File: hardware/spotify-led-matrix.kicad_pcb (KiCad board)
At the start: 2 copper layers, 192.1 x 264.1 mm, 78 parts, among them J1 +5V, J2 DISPLAY_IN, J4 DISPLAY_OUT, J5 USB_C_Receptacle_USB2.0, Q1 IRLML6244TRPBF, Q2 SS8050-G, Q3 SS8050-G, Q4 IRLML6244TRPBF, Q5 IRLML6244TRPBF, Q6 IRLML6244TRPBF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

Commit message: Reorganized files again: Wanted to push to backup everything.
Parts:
- moved Q2 17.8 mm to (85.5, 332.4)
- moved Q3 17.4 mm to (90.5, 332.4)
- moved R20 12.8 mm to (88.0, 336.3), turned to 0 degrees
- moved R19 12.5 mm to (82.0, 333.8), turned to -90 degrees

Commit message: update
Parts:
- moved D2 128.5 mm to (90.5, 390.2)
- moved D4 128.5 mm to (113.1, 390.2)
- moved D8 128.5 mm to (124.5, 390.2)
- moved D3 128.5 mm to (101.8, 390.2)
- moved Q1 128.5 mm to (89.1, 386.7)
- moved Q7 128.5 mm to (123.1, 386.7)
- moved Q8 128.5 mm to (112.1, 386.7)
- moved Q9 128.5 mm to (100.6, 386.7)
- moved R13 128.5 mm to (108.6, 384.2)
- moved R15 128.5 mm to (119.6, 384.1)
- moved R17 128.5 mm to (85.6, 384.2)
- moved R2 128.5 mm to (97.1, 384.1)
- moved R3 128.5 mm to (104.6, 386.2)
- moved R6 128.5 mm to (116.1, 386.1)
- moved R7 128.5 mm to (127.1, 386.2)
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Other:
- board size 192.1 x 264.1 mm -> 192 x 264 mm

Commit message: worked on the layout
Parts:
- moved C10 174.4 mm to (230.3, 251.2), turned to 0 degrees
- moved C6 172.3 mm to (230.3, 267.8), turned to 0 degrees
- moved R12 167.3 mm to (224.1, 280.8), turned to 0 degrees
- moved SW2 167.1 mm to (231.1, 276.1), turned to 90 degrees
- moved SW3 166.9 mm to (231.1, 259.4), turned to 90 degrees
- moved R8 164.9 mm to (224.1, 264.1), turned to 0 degrees
- moved R19 163.8 mm to (181.6, 293.1)
- moved Q2 162.5 mm to (184.0, 292.0)
- moved R20 162.0 mm to (185.4, 295.0)
- moved Q3 160.6 mm to (186.8, 292.1)
- moved C8 154.8 mm to (164.8, 290.5), turned to 90 degrees
- moved C9 150.6 mm to (161.8, 290.5), turned to 90 degrees
- moved J5 150.6 mm to (153.0, 317.0)
- moved C17 147.7 mm to (156.8, 305.0), turned to 0 degrees
- moved C21 147.6 mm to (158.8, 295.9), turned to -90 degrees
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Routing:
- net +3V3: track 0.25 -> 19.4 mm
- net /EN: track 0.00 -> 7.49 mm
- net GND: track 0.00 -> 6.00 mm
- net +5V: track 0.00 -> 6.00 mm
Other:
- board text added: "locked"
- board text removed: "Spotify LED Matrix"
- board text removed: "by Austin Driggs | Fall 2023"

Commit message: more layout stuff
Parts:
- moved R11 6.35 mm to (118.7, 299.8)
- moved R30 6.29 mm to (141.9, 288.9)
- moved R35 6.24 mm to (142.0, 298.2)
- moved C7 6.03 mm to (123.6, 301.3), turned to -90 degrees
- moved R26 5.96 mm to (118.6, 290.4)
- moved Q5 5.88 mm to (137.7, 299.8)
- moved U4 5.77 mm to (128.5, 299.8)
- moved Q4 5.73 mm to (137.6, 290.4)
- moved R31 5.34 mm to (133.3, 299.8)
- moved R29 5.29 mm to (133.2, 290.4)
- moved U3 5.07 mm to (128.4, 290.4)
- moved C12 4.89 mm to (123.6, 292.0)
- moved D6 4.75 mm to (118.7, 296.6)
- moved D5 4.64 mm to (118.6, 287.3)
- moved R20 3.83 mm to (185.2, 291.2)
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
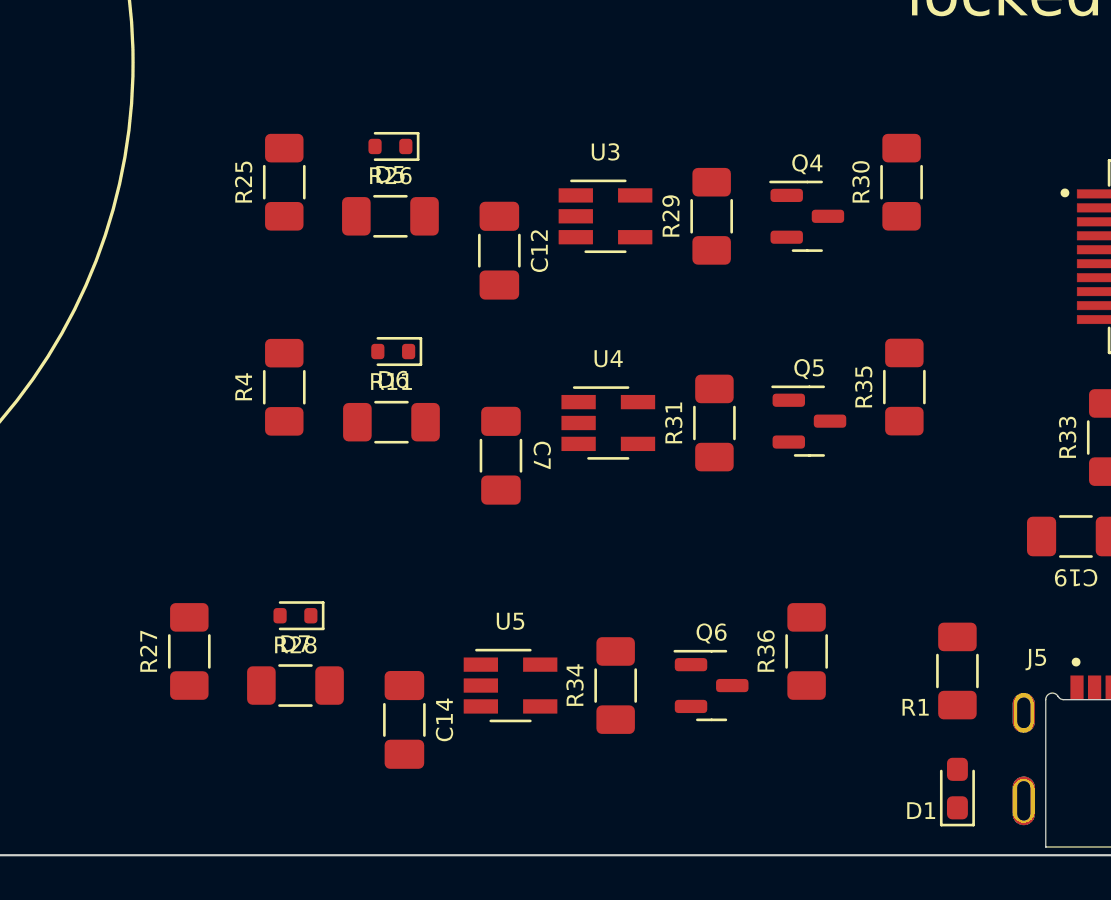
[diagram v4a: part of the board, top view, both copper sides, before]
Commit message: locked layouts
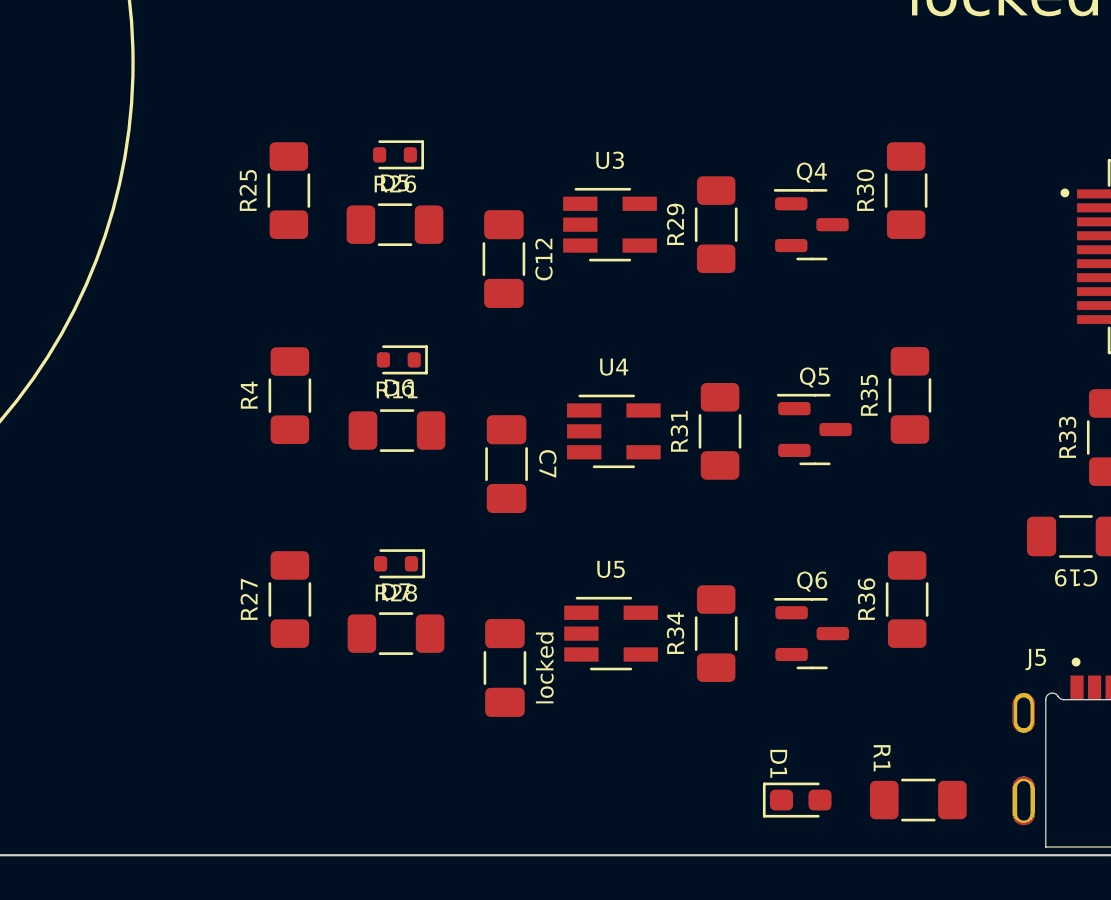
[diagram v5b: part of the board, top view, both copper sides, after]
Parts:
- moved D1 7.14 mm to (137.3, 317.0), turned to 0 degrees
- moved R1 6.13 mm to (142.6, 317.0), turned to 0 degrees
- moved U5 5.15 mm to (128.7, 309.4)
- moved R28 5.15 mm to (118.9, 309.4)
- moved R34 5.15 mm to (133.4, 309.4)
- moved locked 5.15 mm to (123.8, 311.0)
- moved Q6 5.15 mm to (137.8, 309.4)
- moved D7 5.15 mm to (118.9, 306.2)
- moved R27 5.15 mm to (114.0, 307.9)
- moved R36 5.15 mm to (142.1, 307.9)
- moved R31 0.46 mm to (133.6, 300.2)
- moved R4 0.46 mm to (114.0, 298.6)
- moved C7 0.46 mm to (123.9, 301.7)
- moved D6 0.46 mm to (119.0, 297.0)
- moved Q5 0.46 mm to (137.9, 300.1)
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- renumbered C14 to locked

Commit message: locked more
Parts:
- moved C11 1.30 mm to (160.1, 290.5)
- moved C17 1.30 mm to (158.2, 305.0)
- moved C19 1.30 mm to (151.1, 305.0)
- moved C21 1.30 mm to (160.1, 295.9)
- moved C8 1.30 mm to (166.1, 290.5)
- moved C9 1.30 mm to (163.1, 290.5)
- moved J5 1.30 mm to (154.3, 317.0)
- moved R16 1.30 mm to (163.1, 315.2)
- moved R32 1.30 mm to (156.6, 300.5)
- moved R33 1.30 mm to (152.6, 300.5)
- moved U6 1.30 mm to (154.6, 292.3)
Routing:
- net +5V: track 6.00 -> 28.1 mm
- net Net-(D6-K): track 0.00 -> 10.5 mm
- net Net-(D5-K): track 0.00 -> 10.4 mm
- net Net-(D7-K): track 0.00 -> 10.4 mm
- net Net-(Q5-S): track 0.00 -> 7.39 mm
- net Net-(Q4-S): track 0.00 -> 7.39 mm
- net Net-(Q6-S): track 0.00 -> 7.35 mm
- net Net-(D6-A): track 0.00 -> 6.94 mm
- net Net-(D5-A): track 0.00 -> 6.80 mm
- net Net-(D7-A): track 0.00 -> 6.80 mm
- net Net-(D8-K): track 0.00 -> 4.56 mm
- net Net-(D4-K): track 0.00 -> 4.56 mm
- net Net-(D3-K): track 0.00 -> 4.56 mm
- net Net-(D2-K): track 0.00 -> 4.56 mm
- net Net-(D8-A): track 0.00 -> 3.43 mm
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
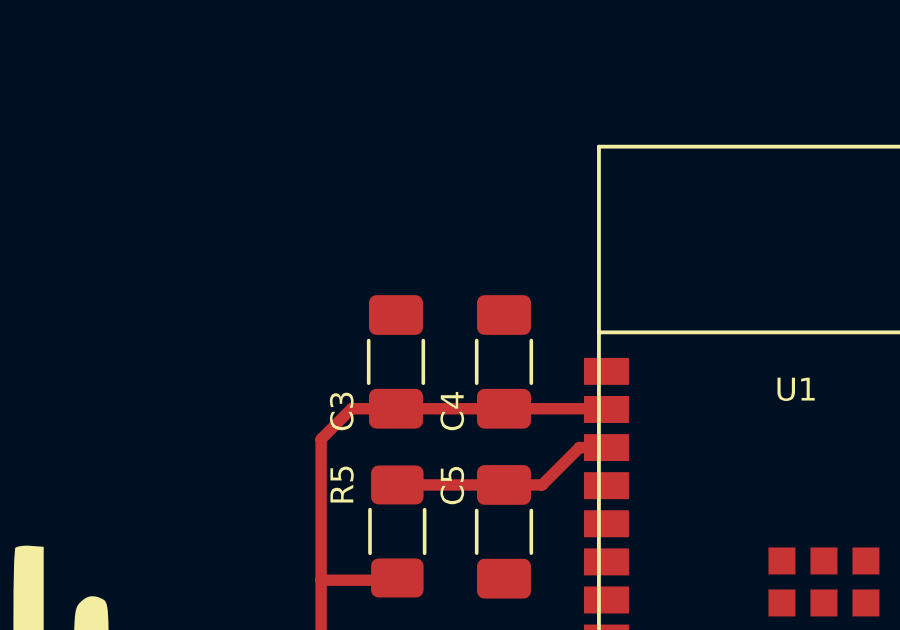
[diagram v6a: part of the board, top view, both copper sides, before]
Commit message: added step files
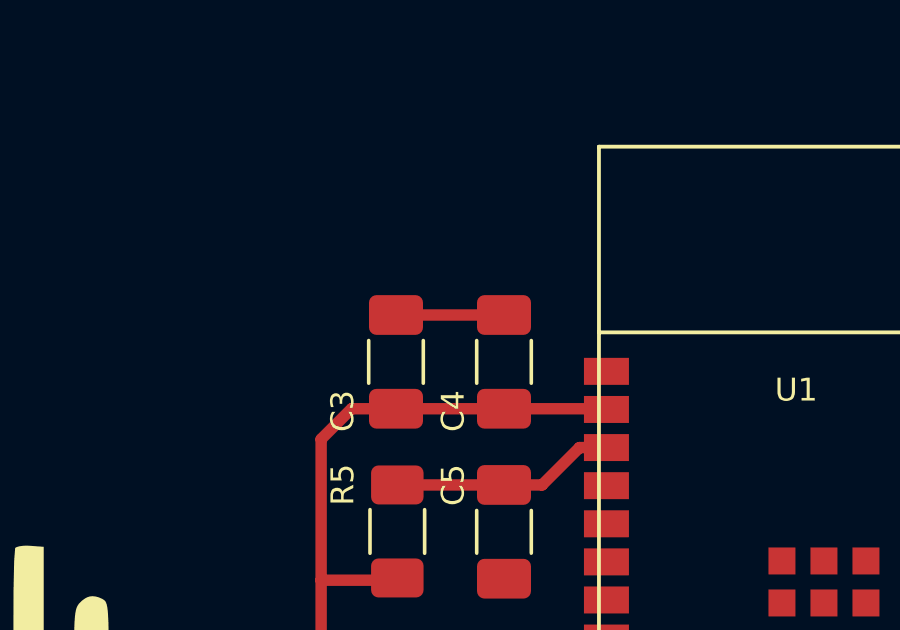
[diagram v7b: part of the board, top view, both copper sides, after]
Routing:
- net GND: track 6.00 -> 9.60 mm
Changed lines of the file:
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@@
     (pad "20" smd roundrect (at 2.47 -2.8575 180) (size 1.97 0.41) (layers "F.Cu" "F.Paste" "F.Mask") (roundrect_rratio 0.02)
       (net 33 "/TXD0") (pinfunction "TXD") (pintype "output") (solder_mask_margin 0.102))
-    (model "${KIPRJMOD}/3dModels/FT231XS-R.step"
+    (model "${KIPRJMOD}/spotify-led-matrix.pretty/FT231XS-R.step"
       (offset (xyz 0 0 0))
       (scale (xyz 1 1 1))
@@
       )
     )
-    (model "${KIPRJMOD}/3dModels/ESP32-WROOM-32E.step"
-      (offset (xyz 0 3 0))
+    (model "${KIPRJMOD}/spotify-led-matrix.pretty/ESP32-S3-WROOM-2.STEP"
+      (offset (xyz 0 -0.1750000056 0))
       (scale (xyz 1 1 1))
-      (rotate (xyz -90 0 0))
+      (rotate (xyz 0 0 0))
     )
   )
@@
     (pad "S2" thru_hole circle locked (at 2.5 -7 180) (size 1.8 1.8) (drill 1.2) (layers "*.Cu" "*.Mask")
       (net 46 "Net-(D5-A)") (pinfunction "S2") (pintype "passive") (solder_mask_margin 0.102))
+    (model "${KIPRJMOD}/spotify-led-matrix.pretty/EVE-YBCAJ008B.stp"
+      (offset (xyz 2.54 -7.62 0))
+      (scale (xyz 1 1 1))
+      (rotate (xyz 0 0 0))
+    )
   )
   (footprint "Resistor_SMD:R_1206_3216Metric_Pad1.30x1.75mm_HandSolder" (layer "F.Cu")
@@
     (pad "C" thru_hole oval locked (at 4.8 -3.25) (size 1.4 3.6) (drill oval 0.8 3) (layers "*.Cu" "*.Mask")
       (net 1 "GND") (pintype "passive") (solder_mask_margin 0.102))
-    (model "${KIPRJMOD}/3dModels/54-00166.step"
+    (model "${KIPRJMOD}/spotify-led-matrix.pretty/54-00166.step"
       (offset (xyz 0 0 0))
       (scale (xyz 1 1 1))
@@
     )
     (stroke (width 0) (type solid)) (fill solid) (layer "F.SilkS"))
-  (gr_rect (start 50.5 55.5) (end 242.5 247.5)
+  (gr_rect locked (start 50.5 55.5) (end 242.5 247.5)
     (stroke (width 0.15) (type default)) (fill none) (layer "F.SilkS"))
   (gr_poly locked
@@
     )
     (stroke (width 0) (type solid)) (fill solid) (layer "F.SilkS"))
-  (gr_line (start 36.5 283.5) (end 256.5 283.5)
+  (gr_line locked (start 36.5 283.5) (end 256.5 283.5)
     (stroke (width 0.15) (type default)) (layer "Dwgs.User"))
-  (gr_line (start 146.5 363.5) (end 146.5 203.5)
+  (gr_line locked (start 146.5 363.5) (end 146.5 203.5)
     (stroke (width 0.15) (type default)) (layer "Dwgs.User"))
-  (gr_arc (start 55.5 319.5) (mid 51.964467 318.035534) (end 50.5 314.5)
+  (gr_arc locked (start 55.5 319.5) (mid 51.964467 318.035534) (end 50.5 314.5)
     (stroke (width 0.1) (type default)) (layer "Edge.Cuts"))
-  (gr_line (start 242.5 314.5) (end 242.5 55.5)
+  (gr_line locked (start 242.5 314.5) (end 242.5 55.5)
     (stroke (width 0.1) (type default)) (layer "Edge.Cuts"))
-  (gr_line (start 50.5 55.5) (end 242.5 55.5)
+  (gr_line locked (start 50.5 55.5) (end 242.5 55.5)
     (stroke (width 0.1) (type default)) (layer "Edge.Cuts"))
-  (gr_arc (start 242.5 314.5) (mid 241.035534 318.035534) (end 237.5 319.5)
+  (gr_arc locked (start 242.5 314.5) (mid 241.035534 318.035534) (end 237.5 319.5)
     (stroke (width 0.1) (type default)) (layer "Edge.Cuts"))
-  (gr_line (start 50.5 314.5) (end 50.5 55.5)
+  (gr_line locked (start 50.5 314.5) (end 50.5 55.5)
     (stroke (width 0.1) (type default)) (layer "Edge.Cuts"))
-  (gr_line (start 55.5 319.5) (end 237.5 319.5)
+  (gr_line locked (start 55.5 319.5) (end 237.5 319.5)
     (stroke (width 0.1) (type default)) (layer "Edge.Cuts"))
   (gr_text locked "by Austin Driggs | Fall 2023" (at 146.558 281.559) (layer "F.SilkS")
@@
     (effects (font (size 4 4) (thickness 0.8) bold) (justify bottom))
   )
-  (dimension (type orthogonal) (layer "Dwgs.User")
+  (dimension locked (type orthogonal) (layer "Dwgs.User")
     (pts (xy 55.5 319.5) (xy 50.5 247.5))
     (height -29.084)
     (orientation 1)
-    (gr_text "2834.6457 mils" (at 26.289 283.5 90) (layer "Dwgs.User")
+    (gr_text locked "2834.6457 mils" (at 26.289 283.5 90) (layer "Dwgs.User")
       (effects (font (size 1 1) (thickness 0.15)))
     )
@@
     (style (thickness 0.15) (arrow_length 1.27) (text_position_mode 2) (extension_height 0.58642) (extension_offset 0.5) keep_text_aligned)
   )
-  (dimension (type orthogonal) (layer "Dwgs.User")
+  (dimension locked (type orthogonal) (layer "Dwgs.User")
     (pts (xy 50.5 55.5) (xy 50.5 247.5))
     (height -24.084)
     (orientation 1)
-    (gr_text "7559.0551 mils" (at 26.289 151.638 90) (layer "Dwgs.User")
+    (gr_text locked "7559.0551 mils" (at 26.289 151.638 90) (layer "Dwgs.User")
       (effects (font (size 1 1) (thickness 0.15)))
     )
@@
     (style (thickness 0.15) (arrow_length 1.27) (text_position_mode 2) (extension_height 0.58642) (extension_offset 0.5) keep_text_aligned)
   )
-  (dimension (type orthogonal) (layer "Dwgs.User")
+  (dimension locked (type orthogonal) (layer "Dwgs.User")
     (pts (xy 55.5 319.5) (xy 50.5 55.5))
     (height -36.831)
     (orientation 1)
-    (gr_text "10393.7008 mils" (at 18.542 187.5 90) (layer "Dwgs.User")
+    (gr_text locked "10393.7008 mils" (at 18.542 187.5 90) (layer "Dwgs.User")
       (effects (font (size 1 1) (thickness 0.15)))
     )
@@
   )
   (segment (start 160.089 288.9455) (end 166.089 288.9455) (width 0.381) (layer "F.Cu") (net 1))
+  (segment (start 184.614 258.752) (end 188.214 258.752) (width 0.381) (layer "F.Cu") (net 1))
   (segment locked (start 189.484 264.417) (end 190.73 263.171) (width 0.381) (layer "F.Cu") (net 4))
   (segment locked (start 184.658 264.417) (end 188.214 264.417) (width 0.381) (layer "F.Cu") (net 4))

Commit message: backup
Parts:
- added TP4: +5V, TestPoint:TestPoint_Loop_D2.54mm_Drill1.5mm_Beaded, F.Cu at (234.2, 294.0)
- added TP5: GND, TestPoint:TestPoint_Loop_D2.54mm_Drill1.5mm_Beaded, F.Cu at (234.2, 299.1)
- added TP6: +3V3, TestPoint:TestPoint_Loop_D2.54mm_Drill1.5mm_Beaded, F.Cu at (238.1, 296.7)
- moved R12 42.0 mm to (182.4, 275.7), turned to -90 degrees
- moved R14 28.4 mm to (215.6, 281.4)
- moved C2 24.8 mm to (210.2, 292.3), turned to -90 degrees
- moved U2 17.6 mm to (216.3, 292.3), turned to 90 degrees
- moved R8 16.6 mm to (215.6, 278.4)
- moved C1 12.3 mm to (222.4, 292.3), turned to 90 degrees
- moved C8 11.7 mm to (164.3, 302.0), turned to 0 degrees
- moved R10 10.2 mm to (185.9, 275.7), turned to -90 degrees
- moved C9 8.59 mm to (164.3, 299.0), turned to 0 degrees
- moved U6 8.10 mm to (162.5, 290.5), turned to -90 degrees
- moved C11 6.92 mm to (164.3, 296.0), turned to 0 degrees
- moved R20 3.74 mm to (188.7, 289.9), turned to -90 degrees
- moved R33 3.42 mm to (153.4, 303.8)
- moved R32 3.38 mm to (155.8, 303.8)
- moved R5 2.96 mm to (185.9, 268.6)
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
